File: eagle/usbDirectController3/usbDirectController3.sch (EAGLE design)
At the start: 37 parts, among them IC1 MCP170312MB, J1 USB_A_SMT_MALE, J5 CORTEX_DEBUG_PTH, Q3 FDD4141TO252, Q4 200mA/50V, U1 ATSAMD21G-A, Y2 32.768kHz

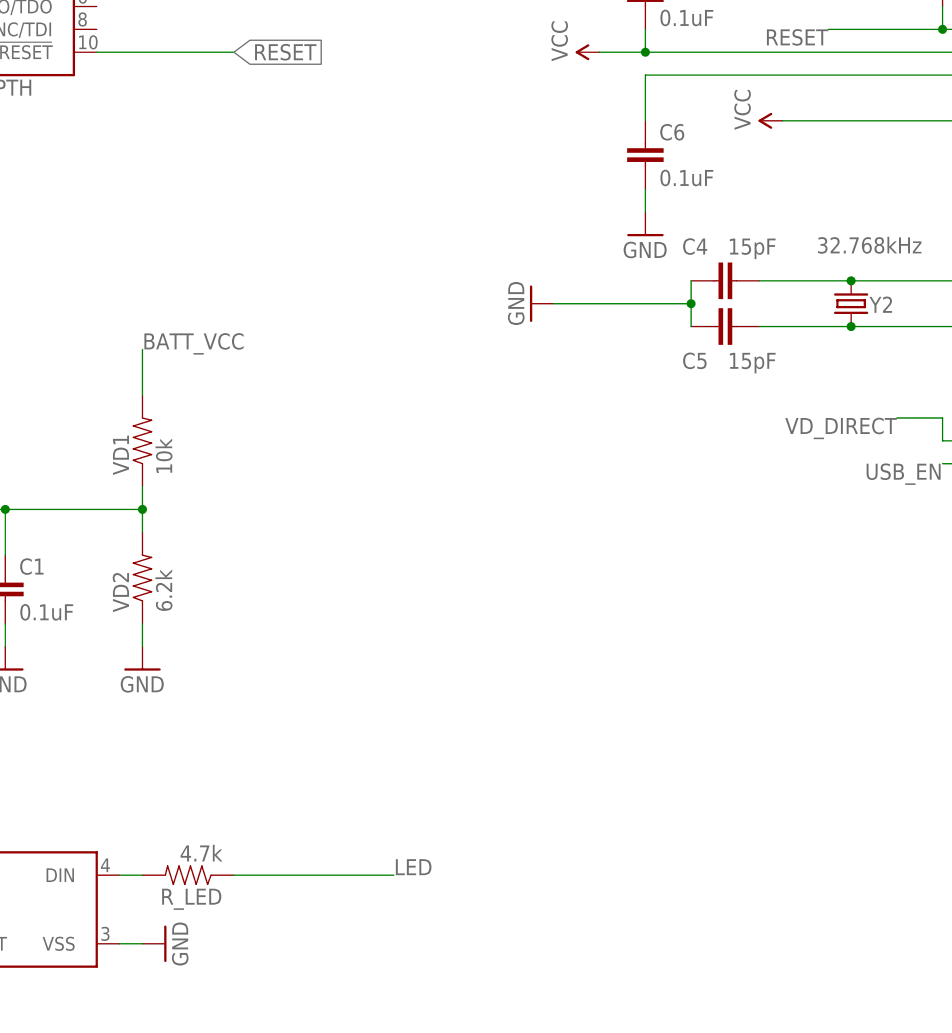
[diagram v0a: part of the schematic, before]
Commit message: UDC3 bugfixes
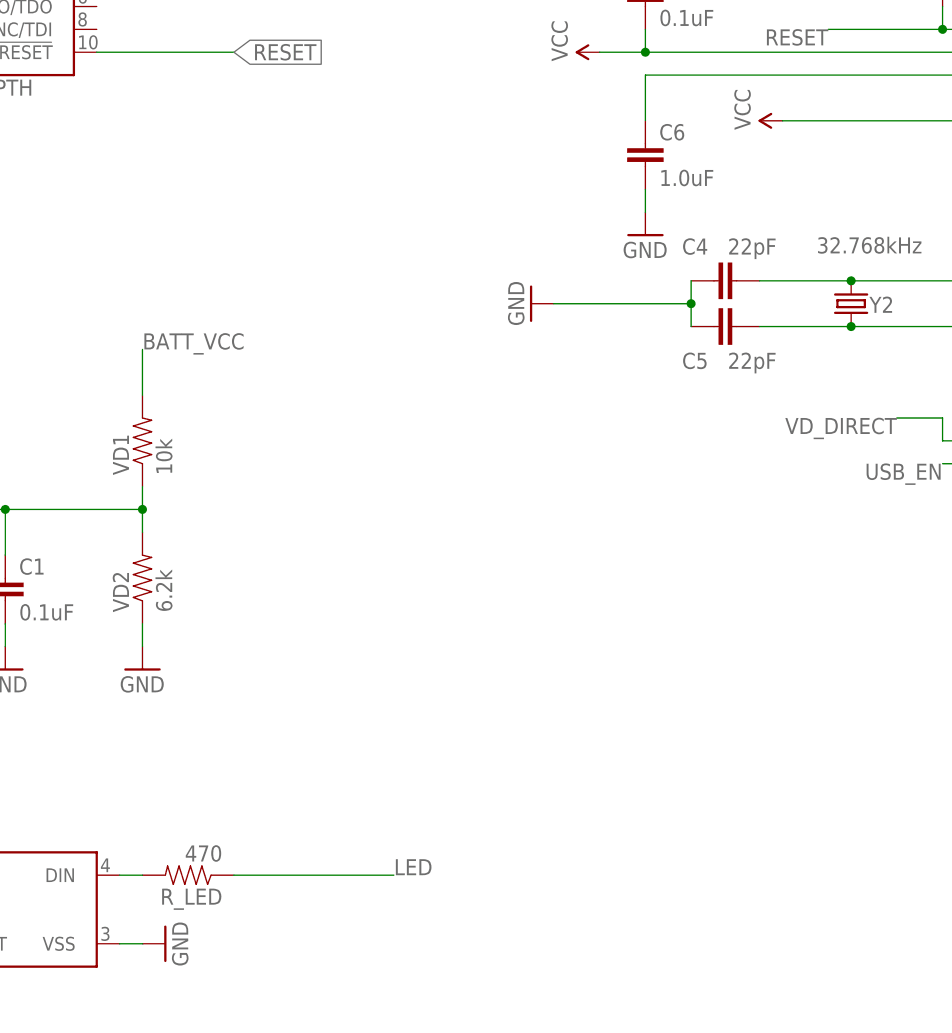
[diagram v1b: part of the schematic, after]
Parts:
- C4, C5: value 15pF -> 22pF
- C6: value 0.1uF -> 1.0uF
- R_LED: value 4.7k -> 470
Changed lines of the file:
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@@
 <grid distance="0.1" unitdist="inch" unit="inch" style="lines" multiple="1" display="no" altdistance="0.01" altunitdist="inch" altunit="inch"/>
 <layers>
-<layer number="1" name="Top" color="4" fill="1" visible="yes" active="no"/>
-<layer number="2" name="Route2" color="1" fill="3" visible="yes" active="no"/>
-<layer number="3" name="Route3" color="4" fill="3" visible="yes" active="no"/>
-<layer number="4" name="Route4" color="1" fill="4" visible="yes" active="no"/>
-<layer number="5" name="Route5" color="4" fill="4" visible="yes" active="no"/>
-<layer number="6" name="Route6" color="1" fill="8" visible="yes" active="no"/>
-<layer number="7" name="Route7" color="4" fill="8" visible="yes" active="no"/>
-<layer number="8" name="Route8" color="1" fill="2" visible="yes" active="no"/>
-<layer number="9" name="Route9" color="4" fill="2" visible="yes" active="no"/>
-<layer number="10" name="Route10" color="1" fill="7" visible="yes" active="no"/>
-<layer number="11" name="Route11" color="4" fill="7" visible="yes" active="no"/>
-<layer number="12" name="Route12" color="1" fill="5" visible="yes" active="no"/>
-<layer number="13" name="Route13" color="4" fill="5" visible="yes" active="no"/>
-<layer number="14" name="Route14" color="1" fill="6" visible="yes" active="no"/>
-<layer number="15" name="Route15" color="4" fill="6" visible="yes" active="no"/>
-<layer number="16" name="Bottom" color="1" fill="1" visible="yes" active="no"/>
-<layer number="17" name="Pads" color="2" fill="1" visible="yes" active="no"/>
-<layer number="18" name="Vias" color="2" fill="1" visible="yes" active="no"/>
-<layer number="19" name="Unrouted" color="6" fill="1" visible="yes" active="no"/>
-<layer number="20" name="Dimension" color="15" fill="1" visible="yes" active="no"/>
-<layer number="21" name="tPlace" color="7" fill="1" visible="yes" active="no"/>
-<layer number="22" name="bPlace" color="7" fill="1" visible="yes" active="no"/>
-<layer number="23" name="tOrigins" color="15" fill="1" visible="yes" active="no"/>
-<layer number="24" name="bOrigins" color="15" fill="1" visible="yes" active="no"/>
-<layer number="25" name="tNames" color="7" fill="1" visible="yes" active="no"/>
-<layer number="26" name="bNames" color="7" fill="1" visible="yes" active="no"/>
-<layer number="27" name="tValues" color="7" fill="1" visible="yes" active="no"/>
-<layer number="28" name="bValues" color="7" fill="1" visible="yes" active="no"/>
+<layer number="1" name="Top" color="4" fill="1" visible="no" active="no"/>
+<layer number="2" name="Route2" color="1" fill="3" visible="no" active="no"/>
+<layer number="3" name="Route3" color="4" fill="3" visible="no" active="no"/>
+<layer number="4" name="Route4" color="1" fill="4" visible="no" active="no"/>
+<layer number="5" name="Route5" color="4" fill="4" visible="no" active="no"/>
+<layer number="6" name="Route6" color="1" fill="8" visible="no" active="no"/>
+<layer number="7" name="Route7" color="4" fill="8" visible="no" active="no"/>
+<layer number="8" name="Route8" color="1" fill="2" visible="no" active="no"/>
+<layer number="9" name="Route9" color="4" fill="2" visible="no" active="no"/>
+<layer number="10" name="Route10" color="1" fill="7" visible="no" active="no"/>
+<layer number="11" name="Route11" color="4" fill="7" visible="no" active="no"/>
+<layer number="12" name="Route12" color="1" fill="5" visible="no" active="no"/>
+<layer number="13" name="Route13" color="4" fill="5" visible="no" active="no"/>
+<layer number="14" name="Route14" color="1" fill="6" visible="no" active="no"/>
+<layer number="15" name="Route15" color="4" fill="6" visible="no" active="no"/>
+<layer number="16" name="Bottom" color="1" fill="1" visible="no" active="no"/>
+<layer number="17" name="Pads" color="2" fill="1" visible="no" active="no"/>
+<layer number="18" name="Vias" color="2" fill="1" visible="no" active="no"/>
+<layer number="19" name="Unrouted" color="6" fill="1" visible="no" active="no"/>
+<layer number="20" name="Dimension" color="15" fill="1" visible="no" active="no"/>
+<layer number="21" name="tPlace" color="7" fill="1" visible="no" active="no"/>
+<layer number="22" name="bPlace" color="7" fill="1" visible="no" active="no"/>
+<layer number="23" name="tOrigins" color="15" fill="1" visible="no" active="no"/>
+<layer number="24" name="bOrigins" color="15" fill="1" visible="no" active="no"/>
+<layer number="25" name="tNames" color="7" fill="1" visible="no" active="no"/>
+<layer number="26" name="bNames" color="7" fill="1" visible="no" active="no"/>
+<layer number="27" name="tValues" color="7" fill="1" visible="no" active="no"/>
+<layer number="28" name="bValues" color="7" fill="1" visible="no" active="no"/>
 <layer number="29" name="tStop" color="7" fill="3" visible="no" active="no"/>
 <layer number="30" name="bStop" color="7" fill="6" visible="no" active="no"/>
@@
 <layer number="35" name="tGlue" color="7" fill="4" visible="no" active="no"/>
 <layer number="36" name="bGlue" color="7" fill="5" visible="no" active="no"/>
-<layer number="37" name="tTest" color="7" fill="1" visible="yes" active="no"/>
-<layer number="38" name="bTest" color="7" fill="1" visible="yes" active="no"/>
+<layer number="37" name="tTest" color="7" fill="1" visible="no" active="no"/>
+<layer number="38" name="bTest" color="7" fill="1" visible="no" active="no"/>
 <layer number="39" name="tKeepout" color="4" fill="11" visible="no" active="no"/>
 <layer number="40" name="bKeepout" color="1" fill="11" visible="no" active="no"/>
@@
 <layer number="44" name="Drills" color="7" fill="1" visible="no" active="no"/>
 <layer number="45" name="Holes" color="7" fill="1" visible="no" active="no"/>
-<layer number="46" name="Milling" color="3" fill="1" visible="yes" active="no"/>
-<layer number="47" name="Measures" color="7" fill="1" visible="yes" active="no"/>
-<layer number="48" name="Document" color="7" fill="1" visible="yes" active="no"/>
-<layer number="49" name="Reference" color="7" fill="1" visible="yes" active="no"/>
-<layer number="50" name="dxf" color="7" fill="1" visible="yes" active="no"/>
-<layer number="51" name="tDocu" color="7" fill="1" visible="yes" active="no"/>
-<layer number="52" name="bDocu" color="7" fill="1" visible="yes" active="no"/>
-<layer number="53" name="tGND_GNDA" color="7" fill="9" visible="yes" active="no"/>
-<layer number="54" name="bGND_GNDA" color="1" fill="9" visible="yes" active="no"/>
-<layer number="56" name="wert" color="7" fill="1" visible="yes" active="no"/>
-<layer number="57" name="tCAD" color="7" fill="1" visible="yes" active="no"/>
-<layer number="59" name="tCarbon" color="7" fill="1" visible="yes" active="no"/>
-<layer number="60" name="bCarbon" color="7" fill="1" visible="yes" active="no"/>
+<layer number="46" name="Milling" color="3" fill="1" visible="no" active="no"/>
+<layer number="47" name="Measures" color="7" fill="1" visible="no" active="no"/>
+<layer number="48" name="Document" color="7" fill="1" visible="no" active="no"/>
+<layer number="49" name="Reference" color="7" fill="1" visible="no" active="no"/>
+<layer number="50" name="dxf" color="7" fill="1" visible="no" active="no"/>
+<layer number="51" name="tDocu" color="7" fill="1" visible="no" active="no"/>
+<layer number="52" name="bDocu" color="7" fill="1" visible="no" active="no"/>
+<layer number="53" name="tGND_GNDA" color="7" fill="9" visible="no" active="no"/>
+<layer number="54" name="bGND_GNDA" color="1" fill="9" visible="no" active="no"/>
+<layer number="56" name="wert" color="7" fill="1" visible="no" active="no"/>
+<layer number="57" name="tCAD" color="7" fill="1" visible="no" active="no"/>
+<layer number="59" name="tCarbon" color="7" fill="1" visible="no" active="no"/>
+<layer number="60" name="bCarbon" color="7" fill="1" visible="no" active="no"/>
 <layer number="88" name="SimResults" color="9" fill="1" visible="yes" active="yes"/>
 <layer number="89" name="SimProbes" color="9" fill="1" visible="yes" active="yes"/>
@@
 <part name="FRAME1" library="frames" deviceset="DINA4_L" device=""/>
 <part name="GND13" library="SparkFun-Aesthetics" deviceset="GND" device=""/>
-<part name="C4" library="SparkFun-Passives" deviceset="CAP" device="0805" value="15pF"/>
-<part name="C5" library="SparkFun-Passives" deviceset="CAP" device="0805" value="15pF"/>
+<part name="C4" library="SparkFun-Passives" deviceset="CAP" device="0805" value="22pF"/>
+<part name="C5" library="SparkFun-Passives" deviceset="CAP" device="0805" value="22pF"/>
 <part name="D2" library="SparkFun-LED" deviceset="WS2812B" device=""/>
 <part name="GND18" library="SparkFun-Aesthetics" deviceset="GND" device=""/>
 <part name="SUPPLY12" library="SparkFun-Aesthetics" deviceset="VCC" device=""/>
-<part name="R_LED" library="SparkFun-Resistors" deviceset="RESISTOR" device="0805-RES" value="4.7k"/>
+<part name="R_LED" library="SparkFun-Resistors" deviceset="RESISTOR" device="0805-RES" value="470"/>
 <part name="R5" library="SparkFun-Passives" deviceset="RESISTOR" device="0805-RES" value="10k"/>
 <part name="GND27" library="SparkFun-Aesthetics" deviceset="GND" device=""/>
@@
 <part name="GND6" library="SparkFun-Aesthetics" deviceset="GND" device=""/>
 <part name="C2" library="SparkFun-Capacitors" library_urn="urn:adsk.eagle:library:510" deviceset="1.0UF" device="-0805-25V-10%" package3d_urn="urn:adsk.eagle:package:37429/1" value="0.1uF"/>
-<part name="C6" library="SparkFun-Capacitors" library_urn="urn:adsk.eagle:library:510" deviceset="1.0UF" device="-0805-25V-10%" package3d_urn="urn:adsk.eagle:package:37429/1" value="0.1uF"/>
+<part name="C6" library="SparkFun-Capacitors" library_urn="urn:adsk.eagle:library:510" deviceset="1.0UF" device="-0805-25V-10%" package3d_urn="urn:adsk.eagle:package:37429/1" value="1.0uF"/>
 <part name="GND7" library="SparkFun-Aesthetics" deviceset="GND" device=""/>
 <part name="Y2" library="samd21-temp" deviceset="CRYSTAL" device="3.2X1.5MM" value="32.768kHz"/>
